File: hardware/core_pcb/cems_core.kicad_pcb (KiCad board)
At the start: 4 copper layers, 211.5 x 85.1 mm, 422 parts, among them J1 24VDC IN, J10 DIGITAL I/O IDC40, J11 BANK B, J13 FIELD 24V A+B, J15 PUMP, J17 RELAY COILS, J18 USB-C, J19 TEMP1, J2 CLIENT, J20 TEMP2, J21 TEMP3, J22 AI 1-2, J23 AI 3-4, J24 AI 5-6, J25 SENSORS, J3 I/O ONLY, J4 RVT70 RiBUS, J5 SWD, J6 SERVICE UART, J7 ROLE, Q1 2N7002, Q2 BC817, Q3 BC807, Q4 2N7002, Q5 BC817, Q6 BC807, SW1 RESET, U1 TPS54360B, U10 APS6404L, U11 MAX6369, U12 74LVC1G08, U13 74LVC1G175, U14 ISO2H823V2.5, U15 ISO808A-1, U16 ISO1I813T, U17 L78L05, U18 ISO7741, U19 74LVC1G08, U2 TLV62569DBV, U20 74LVC1G08, U21 IPS7091S, U22 74LVC1G14, U23 74LVC1G14, U24 LMV331, U25 CPC1017N, U26 CPC1017N, U27 USBLC6-2SC6, U28 ISOW7741, U29 74LVC1G04, U3 STM32H573VIT6, U30 ADS124S08, U31 ISOW7741, U32 74LVC1G04, U33 ITX2424SA, U34 AD4112, U35 L78L05, U36 LM317L, U37 REF5010, U38 LT3045, U4 LAN8742A-CZ, U5 TPD4E05U06, U6 W5500, U7 TPD4E05U06, U8 W25Q128JV, U9 MB85RC1MT, Y1 25MHz, Y2 32.768kHz, Y3 25MHz, Y4 25MHz

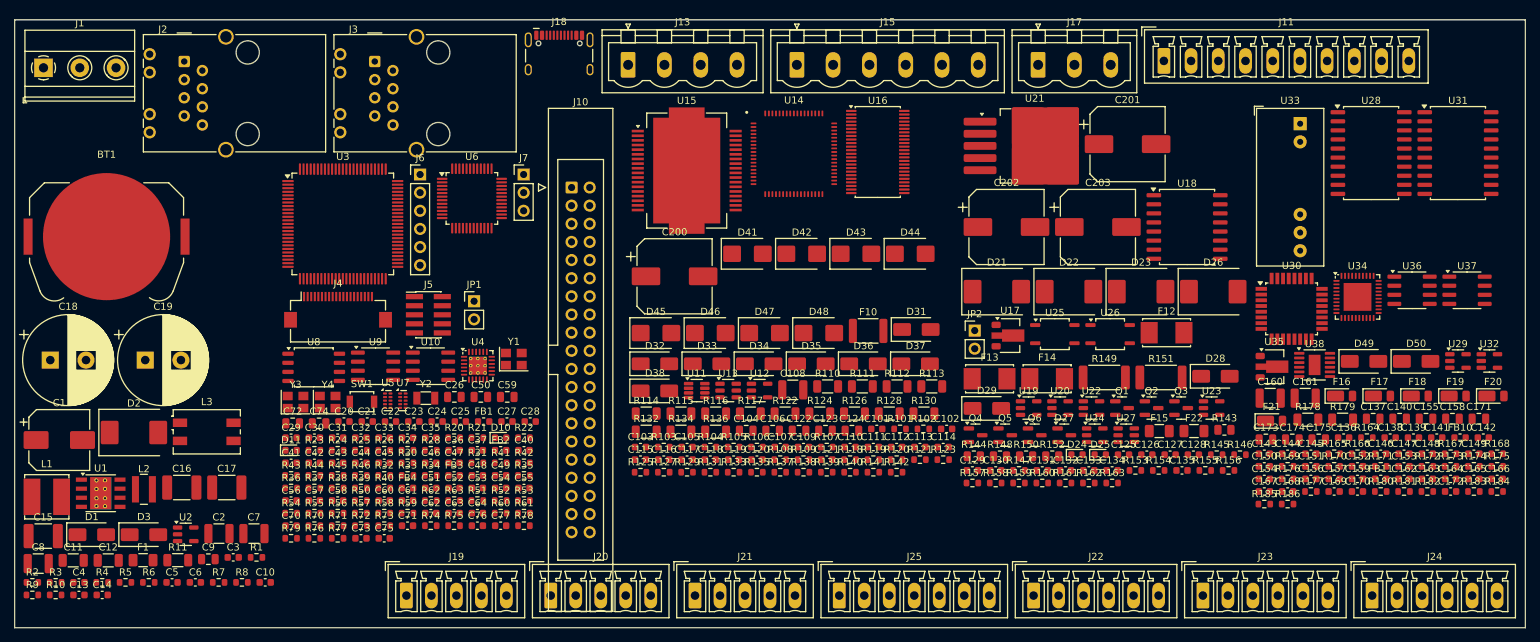
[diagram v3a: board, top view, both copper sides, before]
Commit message: CORE PCB: fit-optional 4 x 4-20 mA analog outputs (AD5755-1, all DNP)
AD5755-1 on the analog island with its own ISOW7741 (CS_AO on PD3) and an ITX2405SA for
the boost converters; keyed 8-way 3.5 mm J26 (keys 2, 6, script-checked). Pin numbers from
the datasheet Table 5. Layout block plan now 2.8 mm over in io_pwr: the board is full
single-sided, see thread for the module option.

Co-Authored-By: Claude Opus 5.5 <noreply@anthropic.com>
Claude-Session: https://claude.ai/code/session_014onnq3eRiDkqdAB6fKiRDW
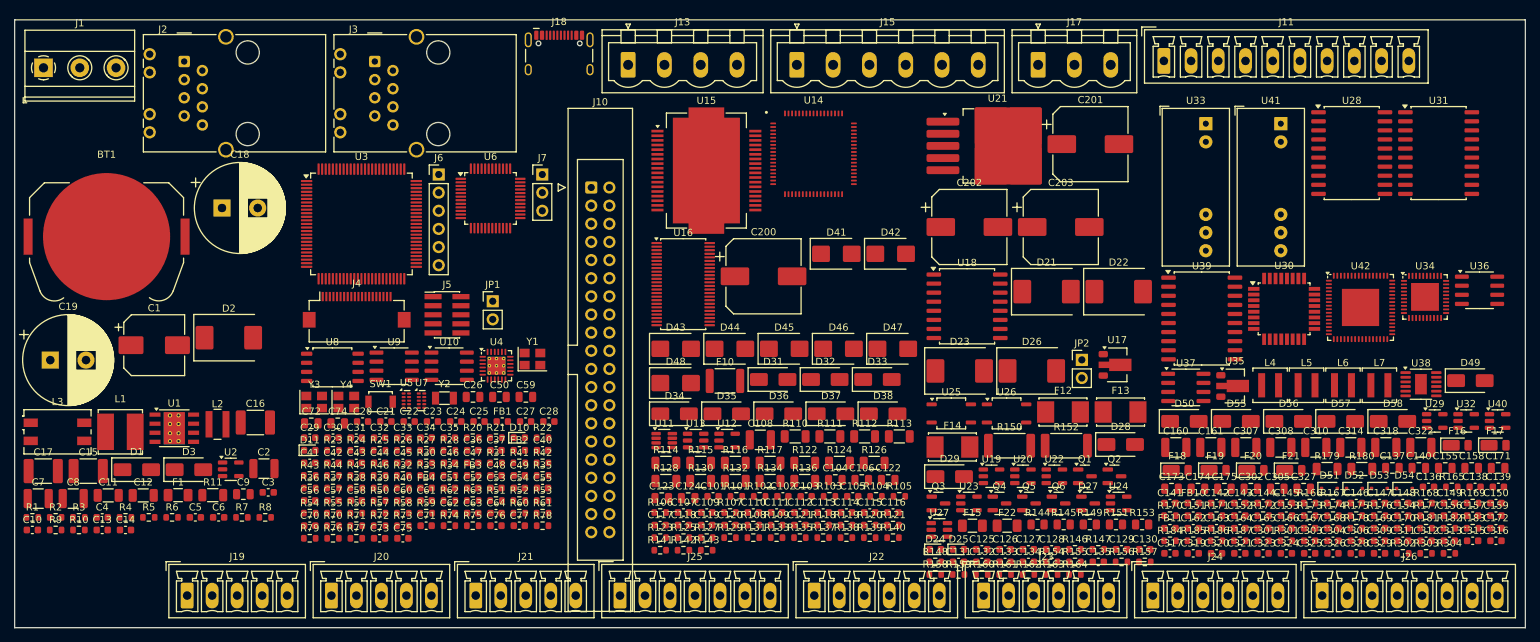
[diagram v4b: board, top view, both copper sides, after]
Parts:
- added C301: 100n, Capacitor_SMD:C_0603_1608Metric, F.Cu at (274.8, 172.9)
- added C302: 10u, Capacitor_SMD:C_0805_2012Metric, F.Cu at (273.1, 165.6)
- added C303: 100n, Capacitor_SMD:C_0603_1608Metric, F.Cu at (281.3, 172.9)
- added C304: 100n, Capacitor_SMD:C_0603_1608Metric, F.Cu at (284.6, 172.9)
- added C305: 10u, Capacitor_SMD:C_0805_2012Metric, F.Cu at (276.8, 165.6)
- added C306: 100n, Capacitor_SMD:C_0603_1608Metric, F.Cu at (287.8, 172.9)
- added C307: 10u 50V, Capacitor_SMD:C_1210_3225Metric, F.Cu at (272.4, 159.9)
- added C308: 22u, Capacitor_SMD:C_1210_3225Metric, F.Cu at (277.3, 159.9)
- added C309: 100n, Capacitor_SMD:C_0603_1608Metric, F.Cu at (291.1, 172.9)
- added C310: 4u7 50V, Capacitor_SMD:C_1210_3225Metric, F.Cu at (282.2, 159.9)
- added C311: 100n 50V, Capacitor_SMD:C_0603_1608Metric, F.Cu at (294.3, 172.9)
- added C312: 10n, Capacitor_SMD:C_0603_1608Metric, F.Cu at (297.6, 172.9)
- added C313: 4n7 50V, Capacitor_SMD:C_0603_1608Metric, F.Cu at (300.9, 172.9)
- added C314: 4u7 50V, Capacitor_SMD:C_1210_3225Metric, F.Cu at (287.1, 159.9)
- added C315: 100n 50V, Capacitor_SMD:C_0603_1608Metric, F.Cu at (304.1, 172.9)
- added C316: 10n, Capacitor_SMD:C_0603_1608Metric, F.Cu at (307.4, 172.9)
- added C317: 4n7 50V, Capacitor_SMD:C_0603_1608Metric, F.Cu at (261.7, 174.7)
- added C318: 4u7 50V, Capacitor_SMD:C_1210_3225Metric, F.Cu at (292.0, 159.9)
- added C319: 100n 50V, Capacitor_SMD:C_0603_1608Metric, F.Cu at (265.0, 174.7)
- added C320: 10n, Capacitor_SMD:C_0603_1608Metric, F.Cu at (268.3, 174.7)
- added C321: 4n7 50V, Capacitor_SMD:C_0603_1608Metric, F.Cu at (271.5, 174.7)
- added C322: 4u7 50V, Capacitor_SMD:C_1210_3225Metric, F.Cu at (296.9, 159.9)
- added C323: 100n 50V, Capacitor_SMD:C_0603_1608Metric, F.Cu at (274.8, 174.7)
- added C324: 10n, Capacitor_SMD:C_0603_1608Metric, F.Cu at (278.0, 174.7)
- added C325: 4n7 50V, Capacitor_SMD:C_0603_1608Metric, F.Cu at (281.3, 174.7)
- added C326: 100n, Capacitor_SMD:C_0603_1608Metric, F.Cu at (284.6, 174.7)
- added C327: 10u, Capacitor_SMD:C_0805_2012Metric, F.Cu at (280.5, 165.6)
- added C328: 100n 50V, Capacitor_SMD:C_0603_1608Metric, F.Cu at (287.8, 174.7)
- added C329: 100n, Capacitor_SMD:C_0603_1608Metric, F.Cu at (291.1, 174.7)
- added D51: PMEG4010, Diode_SMD:D_SOD-323F, F.Cu at (284.1, 165.6)
- added D52: PMEG4010, Diode_SMD:D_SOD-323F, F.Cu at (287.6, 165.6)
- added D53: PMEG4010, Diode_SMD:D_SOD-323F, F.Cu at (291.1, 165.6)
- added D54: PMEG4010, Diode_SMD:D_SOD-323F, F.Cu at (294.6, 165.6)
- added D55: SMAJ33A, Diode_SMD:D_SMA, F.Cu at (271.1, 156.2)
- added D56: SMAJ33A, Diode_SMD:D_SMA, F.Cu at (278.4, 156.2)
- added D57: SMAJ33A, Diode_SMD:D_SMA, F.Cu at (285.7, 156.2)
- added D58: SMAJ33A, Diode_SMD:D_SMA, F.Cu at (293.0, 156.2)
- added J26: AO 1-4, Connector_Phoenix_MC:PhoenixContact_MCV_1,5_8-G-3.5_1x08_P3.50mm_Vertical, F.Cu at (283.1, 180.6)
- added L4: 10uH, Inductor_SMD:L_Coilcraft_XAL4040-XXX, F.Cu at (275.8, 151.2)
- added L5: 10uH, Inductor_SMD:L_Coilcraft_XAL4040-XXX, F.Cu at (280.9, 151.2)
- added L6: 10uH, Inductor_SMD:L_Coilcraft_XAL4040-XXX, F.Cu at (286.0, 151.2)
- added L7: 10uH, Inductor_SMD:L_Coilcraft_XAL4040-XXX, F.Cu at (291.1, 151.2)
- added R187: 1M, Resistor_SMD:R_0603_1608Metric, F.Cu at (271.5, 172.9)
- added R301: 10k, Resistor_SMD:R_0603_1608Metric, F.Cu at (278.0, 172.9)
- added R302: 10k, Resistor_SMD:R_0603_1608Metric, F.Cu at (294.3, 174.7)
- added R303: 10k, Resistor_SMD:R_0603_1608Metric, F.Cu at (297.6, 174.7)
- added R304: 10k, Resistor_SMD:R_0603_1608Metric, F.Cu at (300.9, 174.7)
- added U39: ISOW7741, Package_SO:SOIC-20W_7.5x12.8mm_P1.27mm, F.Cu at (266.2, 141.8)
- added U40: 74LVC1G04, Package_TO_SOT_SMD:SOT-23-5, F.Cu at (307.6, 156.2)
- added U41: ITX2405SA, Converter_DCDC:Converter_DCDC_XP_POWER-ITXxxxxSA_THT, F.Cu at (277.3, 114.5)
- added U42: AD5755-1, Package_CSP:LFCSP-64-1EP_9x9mm_P0.5mm_EP5.21x5.21mm, F.Cu at (288.4, 140.3)
- R143, R148: footprint Resistor_SMD:R_0805_2012Metric -> Resistor_SMD:R_0603_1608Metric
- R145: value 100k -> 10k; footprint Resistor_SMD:R_0603_1608Metric -> Resistor_SMD:R_0805_2012Metric
- R147: value 10k -> 100k
- R149, R151: value 1k 1W -> 10k; footprint Resistor_SMD:R_2512_6332Metric -> Resistor_SMD:R_0805_2012Metric
- R150, R152: value 10k -> 1k 1W; footprint Resistor_SMD:R_0805_2012Metric -> Resistor_SMD:R_2512_6332Metric
- R153: footprint Resistor_SMD:R_0603_1608Metric -> Resistor_SMD:R_0805_2012Metric
- R154: value 4k3 -> 10k
- R155: value 10k -> 4k3
- R156: value 1M -> 10k
- R157: value 4k7 -> 1M
- R158: value 330R -> 4k7
- R160: value 5k1 -> 330R
- R162: value 33k -> 5k1
- R163: value 68k -> 33k
- R164: value 10k -> 68k
- R166: value 5k11 0.1% -> 10k
- R167: value 10M -> 5k11 0.1%
- R173: value 100R -> 10M
- R176: value 10k -> 100R
- R178: value 250R 0.1% -> 10k; footprint Resistor_SMD:R_1206_3216Metric -> Resistor_SMD:R_0603_1608Metric
- R180: value 100k -> 250R 0.1%; footprint Resistor_SMD:R_0603_1608Metric -> Resistor_SMD:R_1206_3216Metric
- R181: value 240R 1% -> 100k
- R182: value 2k26 1% -> 240R 1%
- R183: value 3k -> 2k26 1%
- R184: value 100k 0.1% -> 3k
- R186: value 1M -> 100k 0.1%
- moved R143 74.4 mm to (196.9, 174.2)
- moved R184 46.3 mm to (261.7, 172.9)
- moved R164 45.1 mm to (248.4, 177.6)
- moved U37 41.7 mm to (264.0, 151.5)
- moved R123 41.1 mm to (190.4, 172.5)
- moved C141 38.5 mm to (261.7, 167.6)
- moved C142 38.5 mm to (268.3, 167.6)
- moved FB10 38.5 mm to (265.0, 167.6)
- moved Q3 36.5 mm to (229.3, 167.7)
- moved U23 36.5 mm to (233.6, 167.7)
- moved F19 35.2 mm to (268.1, 163.1)
- moved F18 35.2 mm to (262.8, 163.1)
- moved F20 35.2 mm to (273.4, 163.1)
- moved D50 33.5 mm to (263.8, 156.2)
- moved C10 33.4 mm to (102.5, 171.4)
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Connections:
- R143 pad 1: +24V_FA -> +3V3
- R143 pad 2: FA_LED_A -> CS_AO
- R144 pad 1: +24V_FB -> +24V_FA
- R144 pad 2: FB_LED_A -> FA_LED_A
- R145 pad 1: PUMP_EN -> +24V_FB
- R145 pad 2: GND -> FB_LED_A
- R146 pad 1: PUMP_PWM -> PUMP_EN
- R147 pad 1: +5V_P -> PUMP_PWM
- R147 pad 2: P_DG -> GND
- R148 pad 1: +24V_FA -> +5V_P
- R148 pad 2: P_PWM_B -> P_DG
- R149 pad 1: P_PWM_E -> +24V_FA
- R149 pad 2: P_PWM_OUT -> P_PWM_B
- R150 pad 1: +24V_FA -> P_PWM_E
- R150 pad 2: P_DIR_B -> P_PWM_OUT
- R151 pad 1: P_DIR_E -> +24V_FA
- R151 pad 2: P_DIR_OUT -> P_DIR_B
- R152 pad 1: P_TACH_IN -> P_DIR_E
- R152 pad 2: P_TACH_C -> P_DIR_OUT
- R153 pad 1: +5V_P -> P_TACH_IN
- R153 pad 2: P_TREF -> P_TACH_C
- R154 pad 1: P_TREF -> +5V_P
- R154 pad 2: FIELD_0V -> P_TREF
- R155 pad 1: +5V_P -> P_TREF
- R155 pad 2: P_TACH_F -> FIELD_0V
- R156 pad 1: P_TACH_F -> +5V_P
- R156 pad 2: P_TACH_C -> P_TACH_F
- R157 pad 1: +5V_P -> P_TACH_F
- R157 pad 2: P_TACH_PU -> P_TACH_C
- R158 pad 1: GATE -> +5V_P
- R158 pad 2: REL1_A -> P_TACH_PU
- R159 pad 2: REL2_A -> REL1_A
- R160 pad 1: USB_CC1 -> GATE
- R160 pad 2: GND -> REL2_A
- R161 pad 1: USB_CC2 -> USB_CC1
- R162 pad 1: VBUS_USB -> USB_CC2
- R162 pad 2: USB_VBUS_SNS -> GND
- R163 pad 1: USB_VBUS_SNS -> VBUS_USB
- R163 pad 2: GND -> USB_VBUS_SNS
- R164 pad 1: +3V3 -> USB_VBUS_SNS
- R164 pad 2: T_ENFLT -> GND
- R165 pad 1: +3V3_T -> +3V3
- R165 pad 2: T_RST -> T_ENFLT
- R166 pad 1: T_REFP -> +3V3_T
- R166 pad 2: GND_T -> T_RST
- R167 pad 1: T1_N -> T_REFP
- R167 pad 2: T_AINCOM -> GND_T
- R168 pad 1: T2_N -> T1_N
- R169 pad 1: T3_N -> T2_N
- R170 pad 1: T4_N -> T3_N
- R171 pad 1: T5_N -> T4_N
- R172 pad 1: T6_N -> T5_N
- R173 pad 1: T_RTN1 -> T6_N
- R173 pad 2: T_REFP -> T_AINCOM
- R174 pad 1: T_RTN2 -> T_RTN1
- R175 pad 1: T_RTN3 -> T_RTN2
- R176 pad 1: +3V3 -> T_RTN3
- R176 pad 2: AI_ENFLT -> T_REFP
- R177 pad 1: +5V_AI -> +3V3
- R177 pad 2: AI_ERR -> AI_ENFLT
- R178 pad 1: AI5_IN -> +5V_AI
- R178 pad 2: GND_AI -> AI_ERR
- R179 pad 1: AI6_IN -> AI5_IN
- R180 pad 1: LVL_SIG -> AI6_IN
- R181 pad 1: +13V_AI -> LVL_SIG
- R181 pad 2: AI_ADJ -> GND_AI
- R182 pad 1: AI_ADJ -> +13V_AI
- R182 pad 2: GND_AI -> AI_ADJ
- R183 pad 1: FLOW_ILIM -> AI_ADJ
- R184 pad 1: +10V_FLOW -> FLOW_ILIM
- R184 pad 2: V10_MON -> GND_AI
- R185 pad 1: V10_MON -> +10V_FLOW
- R185 pad 2: GND_AI -> V10_MON
- R186 pad 1: FLOW_SIG -> V10_MON
- U3 pad 84: (no net) -> CS_AO

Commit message: CORE PCB: SPI expansion header J26 for plug-on modules; analog outputs move off the core
Gary: analog out as an add-on module. J26 10-way latched IDC: +24 V and +3.3 V behind PTCs,
SPI4 through 100R, MISO buffered by a 74LVC1G125 enabled by CS_EXP (PD3), EXP_INT on PD7.
The AD5755-1 block drafted in 04adb9f is removed from the core and will become the module.
Layout block plan fits again. CORE_PCB.md section 16.

Co-Authored-By: Claude Opus 5.5 <noreply@anthropic.com>
Claude-Session: https://claude.ai/code/session_014onnq3eRiDkqdAB6fKiRDW
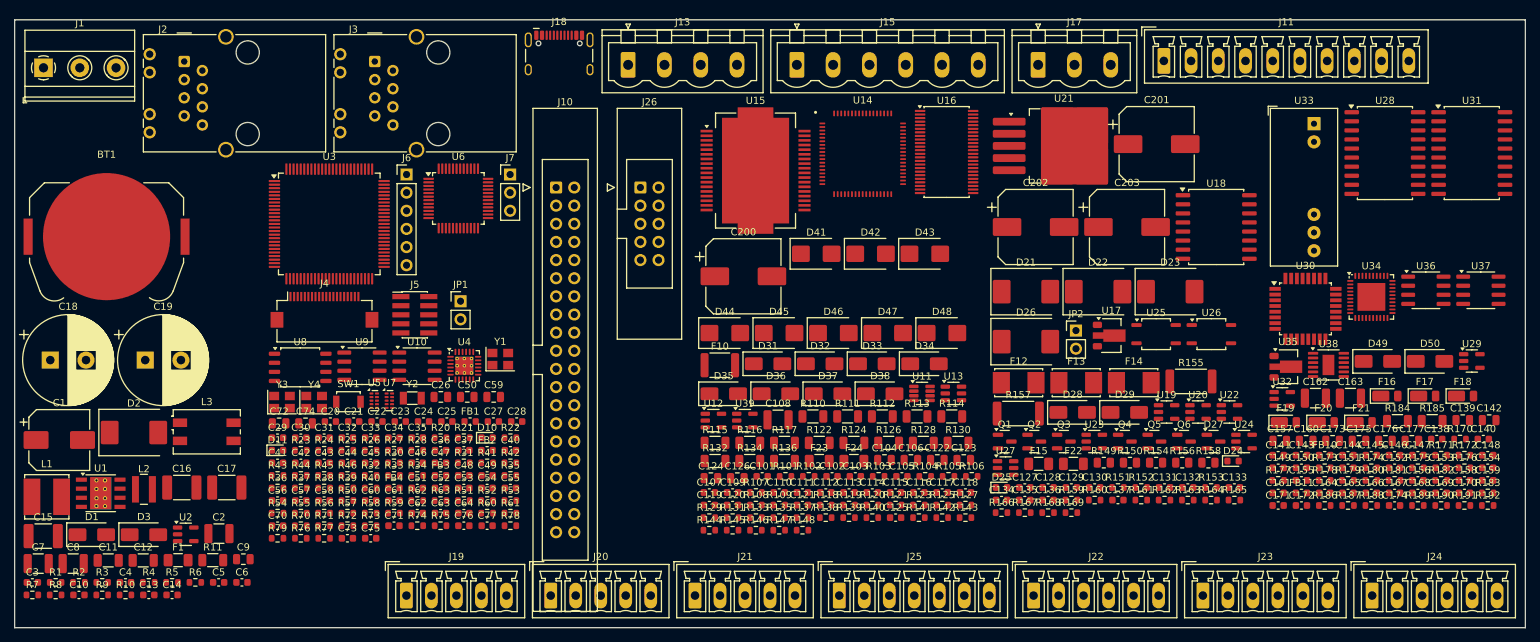
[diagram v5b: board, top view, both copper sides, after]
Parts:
- removed C301, C303, C304, C306, C309, C326, C329: 100n, Capacitor_SMD:C_0603_1608Metric
- removed C302, C305, C327: 10u, Capacitor_SMD:C_0805_2012Metric
- removed C307: 10u 50V, Capacitor_SMD:C_1210_3225Metric
- removed C308: 22u, Capacitor_SMD:C_1210_3225Metric
- removed C310, C314, C318, C322: 4u7 50V, Capacitor_SMD:C_1210_3225Metric
- removed C311, C315, C319, C323, C328: 100n 50V, Capacitor_SMD:C_0603_1608Metric
- removed C312, C316, C320, C324: 10n, Capacitor_SMD:C_0603_1608Metric
- removed C313, C317, C321, C325: 4n7 50V, Capacitor_SMD:C_0603_1608Metric
- removed D51, D52, D53, D54: PMEG4010, Diode_SMD:D_SOD-323F
- removed D55, D56, D57, D58: SMAJ33A, Diode_SMD:D_SMA
- removed L4, L5, L6, L7: 10uH, Inductor_SMD:L_Coilcraft_XAL4040-XXX
- removed R301, R302, R303, R304: 10k, Resistor_SMD:R_0603_1608Metric
- removed U40: 74LVC1G04, Package_TO_SOT_SMD:SOT-23-5
- removed U41: ITX2405SA, Converter_DCDC:Converter_DCDC_XP_POWER-ITXxxxxSA_THT
- removed U42: AD5755-1, Package_CSP:LFCSP-64-1EP_9x9mm_P0.5mm_EP5.21x5.21mm
- added C176: 4u7 25V, Capacitor_SMD:C_0805_2012Metric, F.Cu at (291.9, 158.9)
- added C177: 10u 25V, Capacitor_SMD:C_0805_2012Metric, F.Cu at (295.6, 158.9)
- added F23: 0.5A, Fuse:Fuse_1206_3216Metric, F.Cu at (212.6, 161.8)
- added F24: 0.1A, Fuse:Fuse_1206_3216Metric, F.Cu at (217.5, 161.8)
- added R188: 2k26 1%, Resistor_SMD:R_0603_1608Metric, F.Cu at (289.9, 168.0)
- added R189: 3k, Resistor_SMD:R_0603_1608Metric, F.Cu at (296.5, 168.0)
- added R190: 100k 0.1%, Resistor_SMD:R_0603_1608Metric, F.Cu at (299.7, 168.0)
- added R191: 100k 0.1%, Resistor_SMD:R_0603_1608Metric, F.Cu at (303.0, 168.0)
- added R192: 1M, Resistor_SMD:R_0603_1608Metric, F.Cu at (306.2, 168.0)
- C125: value 330n 50V -> 100n
- C126: value 1u -> 100n; footprint Capacitor_SMD:C_0603_1608Metric -> Capacitor_SMD:C_0805_2012Metric
- C127: value 100n -> 330n 50V
- C128, C147: value 100n -> 1u
- C131: value 100n 50V -> 100n
- C133: value 100n -> 100n 50V
- C134: value 1n -> 100n
- C136: value 100n -> 1n
- C137, C140, C158: value 10u -> 100n; footprint Capacitor_SMD:C_0805_2012Metric -> Capacitor_SMD:C_0603_1608Metric
- C139, C142, C157: value 100n -> 10u; footprint Capacitor_SMD:C_0603_1608Metric -> Capacitor_SMD:C_0805_2012Metric
- C143, C170: value 1u -> 100n
- C148, C149: value 10n C0G -> 100n
- C154: value 100n -> 10n C0G
- C155: value 10u -> 10n C0G; footprint Capacitor_SMD:C_0805_2012Metric -> Capacitor_SMD:C_0603_1608Metric
- C160: value 10u 50V -> 10u; footprint Capacitor_SMD:C_1210_3225Metric -> Capacitor_SMD:C_0805_2012Metric
- C161: value 10u 50V -> 100n; footprint Capacitor_SMD:C_1210_3225Metric -> Capacitor_SMD:C_0603_1608Metric
- C162: value 100n -> 10u 50V; footprint Capacitor_SMD:C_0603_1608Metric -> Capacitor_SMD:C_1210_3225Metric
- C163: value 1u -> 10u 50V; footprint Capacitor_SMD:C_0603_1608Metric -> Capacitor_SMD:C_1210_3225Metric
- C169: value 330n 50V -> 1u
- C171: value 1u 25V -> 330n 50V; footprint Capacitor_SMD:C_0805_2012Metric -> Capacitor_SMD:C_0603_1608Metric
- C174: value 4u7 25V -> 1u; footprint Capacitor_SMD:C_0805_2012Metric -> Capacitor_SMD:C_0603_1608Metric
- C175: value 10u 25V -> 1u 25V
- J26: value AO 1-4 -> SPI EXPANSION; footprint Connector_Phoenix_MC:PhoenixContact_MCV_1,5_8-G-3.5_1x08_P3.50mm_Vertical -> Connector_IDC:IDC-Header_2x05_P2.54mm_Latch_Vertical
- R138, R139, R140: value 10k -> 100R
- R141: value 10k -> 100k
- R144, R145, R153: footprint Resistor_SMD:R_0805_2012Metric -> Resistor_SMD:R_0603_1608Metric
- R146, R147: value 100k -> 10k
- R150: value 1k 1W -> 10k; footprint Resistor_SMD:R_2512_6332Metric -> Resistor_SMD:R_0805_2012Metric
- R151: value 10k -> 100k; footprint Resistor_SMD:R_0805_2012Metric -> Resistor_SMD:R_0603_1608Metric
- R152: value 1k 1W -> 100k; footprint Resistor_SMD:R_2512_6332Metric -> Resistor_SMD:R_0603_1608Metric
- R154, R156: footprint Resistor_SMD:R_0603_1608Metric -> Resistor_SMD:R_0805_2012Metric
- R155: value 4k3 -> 1k 1W; footprint Resistor_SMD:R_0603_1608Metric -> Resistor_SMD:R_2512_6332Metric
- R157: value 1M -> 1k 1W; footprint Resistor_SMD:R_0603_1608Metric -> Resistor_SMD:R_2512_6332Metric
- R158: value 4k7 -> 10k; footprint Resistor_SMD:R_0603_1608Metric -> Resistor_SMD:R_0805_2012Metric
- R159: value 330R -> 10k
- R160: value 330R -> 4k3
- R161: value 5k1 -> 10k
- R162: value 5k1 -> 1M
- R163: value 33k -> 4k7
- R164: value 68k -> 330R
- R165: value 10k -> 330R
- R166: value 10k -> 5k1
- R167: value 5k11 0.1% -> 5k1
- R168: value 10M -> 33k
- R169: value 10M -> 68k
- R170, R171: value 10M -> 10k
- R172: value 10M -> 5k11 0.1%
- R174, R175, R176: value 100R -> 10M
- R177, R178: value 10k -> 10M
- R179, R180: value 250R 0.1% -> 100R; footprint Resistor_SMD:R_1206_3216Metric -> Resistor_SMD:R_0603_1608Metric
- R181: value 100k -> 100R
- R182: value 240R 1% -> 10k
- R183: value 2k26 1% -> 10k
- R184: value 3k -> 250R 0.1%; footprint Resistor_SMD:R_0603_1608Metric -> Resistor_SMD:R_1206_3216Metric
- R185: value 100k 0.1% -> 250R 0.1%; footprint Resistor_SMD:R_0603_1608Metric -> Resistor_SMD:R_1206_3216Metric
- R186: value 100k 0.1% -> 100k
- R187: value 1M -> 240R 1%
- U39: value ISOW7741 -> 74LVC1G125; footprint Package_SO:SOIC-20W_7.5x12.8mm_P1.27mm -> Package_TO_SOT_SMD:SOT-23-5
- moved J26 111.2 mm to (187.6, 123.5)
- moved U39 65.5 mm to (202.2, 156.1)
- moved R169 56.2 mm to (247.9, 169.0)
- moved C136 53.3 mm to (244.7, 167.2)
- moved R168 52.9 mm to (244.7, 169.0)
- moved R145 46.4 mm to (200.5, 171.4)
- moved R144 46.0 mm to (197.3, 171.4)
- moved R146 44.8 mm to (203.8, 171.4)
- moved R147 44.8 mm to (207.0, 171.4)
- moved R106 43.9 mm to (234.0, 163.9)
- moved D24 43.5 mm to (270.6, 161.8)
- moved U37 43.5 mm to (305.3, 137.9)
- moved R166 43.2 mm to (238.2, 169.0)
- moved R167 43.2 mm to (241.4, 169.0)
- moved C123 42.6 mm to (232.9, 161.6)
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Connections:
- C125 pad 1: +24V_FA -> +3V3
- C125 pad 2: FIELD_0V -> GND
- C126 pad 1: +5V_P -> +24V_EXP
- C126 pad 2: FIELD_0V -> GND
- C127 pad 1: +3V3 -> +24V_FA
- C127 pad 2: GND -> FIELD_0V
- C128 pad 1: +3V3 -> +5V_P
- C128 pad 2: GND -> FIELD_0V
- C130 pad 1: +5V_P -> +3V3
- C130 pad 2: FIELD_0V -> GND
- C131 pad 1: +24V_FP -> +3V3
- C131 pad 2: FIELD_0V -> GND
- C133 pad 1: +5V_P -> +24V_FP
- C134 pad 1: P_TACH_C -> +5V_P
- C136 pad 1: +3V3 -> P_TACH_C
- C136 pad 2: GND -> FIELD_0V
- C137 pad 1: +5V -> +5V_P
- C137 pad 2: GND -> FIELD_0V
- C138 pad 1: +5V -> +3V3
- C139 pad 1: +3V3 -> +5V
- C140 pad 1: +3V3_T -> +5V
- C140 pad 2: GND_T -> GND
- C141 pad 1: +3V3_T -> +3V3
- C141 pad 2: GND_T -> GND
- C143 pad 1: +3V3_TA -> +3V3_T
- C144 pad 1: +3V3_TA -> +3V3_T
- C145 pad 1: T_REFOUT -> +3V3_TA
- C146 pad 1: T_REFP -> +3V3_TA
- C147 pad 1: T_AINCOM -> T_REFOUT
- C148 pad 1: T1_P -> T_REFP
- C148 pad 2: T1_N -> GND_T
- C149 pad 1: T2_P -> T_AINCOM
- C149 pad 2: T2_N -> GND_T
- C150 pad 1: T3_P -> T1_P
- C150 pad 2: T3_N -> T1_N
- C151 pad 1: T4_P -> T2_P
- C151 pad 2: T4_N -> T2_N
- C152 pad 1: T5_P -> T3_P
- C152 pad 2: T5_N -> T3_N
- C153 pad 1: T6_P -> T4_P
- C153 pad 2: T6_N -> T4_N
- C154 pad 1: +3V3 -> T5_P
- C154 pad 2: GND -> T5_N
- C155 pad 1: +5V -> T6_P
- C155 pad 2: GND -> T6_N
- C156 pad 1: +5V -> +3V3
- C157 pad 1: +3V3 -> +5V
- C158 pad 1: +5V_AI -> +5V
- C158 pad 2: GND_AI -> GND
- C159 pad 1: +5V_AI -> +3V3
- C159 pad 2: GND_AI -> GND
- C160 pad 1: +24V -> +5V_AI
- C160 pad 2: GND -> GND_AI
- C161 pad 1: +24V_AI -> +5V_AI
- C162 pad 1: +5V_AI -> +24V
- C162 pad 2: GND_AI -> GND
- C163 pad 1: +5V_AIA -> +24V_AI
- C164 pad 1: +5V_AIA -> +5V_AI
- C165 pad 1: AI_REGCAPA -> +5V_AIA
- C166 pad 1: AI_REGCAPA -> +5V_AIA
- C167 pad 1: AI_REGCAPD -> AI_REGCAPA
- C168 pad 1: AI_REF -> AI_REGCAPA
- C169 pad 1: +24V_AI -> AI_REGCAPD
- C170 pad 1: +5V_LVL -> AI_REF
- C171 pad 1: +13V_AI -> +24V_AI
- C172 pad 1: REF10_NR -> +5V_LVL
- C173 pad 1: REF10 -> +13V_AI
- C174 pad 1: +13V_AI -> REF10_NR
- C175 pad 1: +10V_FLOW -> REF10
- J26 pad 1: AO_IOUT1 -> +24V_EXP
- J26 pad 2: GND_AI -> GND
- J26 pad 3: AO_IOUT2 -> +3V3_EXP
- J26 pad 4: GND_AI -> GND
- J26 pad 5: AO_IOUT3 -> EXP_SCK
- J26 pad 6: GND_AI -> GND
- J26 pad 7: AO_IOUT4 -> EXP_MOSI
- J26 pad 8: GND_AI -> EXP_MISO
- R138 pad 1: +3V3 -> SPI4_SCK
- R138 pad 2: CS_A -> EXP_SCK
- R139 pad 1: +3V3 -> SPI4_MOSI
- R139 pad 2: CS_B -> EXP_MOSI
- R140 pad 1: +3V3 -> CS_EXP
- R140 pad 2: CS_IN -> EXP_CS
- R141 pad 1: +3V3 -> EXP_MISO
- R141 pad 2: CS_T -> GND
- R142 pad 2: CS_AI -> EXP_INT
- R143 pad 2: CS_AO -> CS_A
- R144 pad 1: +24V_FA -> +3V3
- R144 pad 2: FA_LED_A -> CS_B
- R145 pad 1: +24V_FB -> +3V3
- R145 pad 2: FB_LED_A -> CS_IN
- R146 pad 1: PUMP_EN -> +3V3
- R146 pad 2: GND -> CS_T
- R147 pad 1: PUMP_PWM -> +3V3
- R147 pad 2: GND -> CS_AI
- R148 pad 1: +5V_P -> +3V3
- R148 pad 2: P_DG -> CS_EXP
- R149 pad 2: P_PWM_B -> FA_LED_A
- R150 pad 1: P_PWM_E -> +24V_FB
- R150 pad 2: P_PWM_OUT -> FB_LED_A
- R151 pad 1: +24V_FA -> PUMP_EN
- R151 pad 2: P_DIR_B -> GND
- R152 pad 1: P_DIR_E -> PUMP_PWM
- R152 pad 2: P_DIR_OUT -> GND
- R153 pad 1: P_TACH_IN -> +5V_P
- R153 pad 2: P_TACH_C -> P_DG
- R154 pad 1: +5V_P -> +24V_FA
- R154 pad 2: P_TREF -> P_PWM_B
- R155 pad 1: P_TREF -> P_PWM_E
- R155 pad 2: FIELD_0V -> P_PWM_OUT
- R156 pad 1: +5V_P -> +24V_FA
- R156 pad 2: P_TACH_F -> P_DIR_B
- R157 pad 1: P_TACH_F -> P_DIR_E
- R157 pad 2: P_TACH_C -> P_DIR_OUT
- R158 pad 1: +5V_P -> P_TACH_IN
- R158 pad 2: P_TACH_PU -> P_TACH_C
- R159 pad 1: GATE -> +5V_P
- R159 pad 2: REL1_A -> P_TREF
- R160 pad 1: GATE -> P_TREF
- R160 pad 2: REL2_A -> FIELD_0V
- R161 pad 1: USB_CC1 -> +5V_P
- R161 pad 2: GND -> P_TACH_F
- R162 pad 1: USB_CC2 -> P_TACH_F
- R162 pad 2: GND -> P_TACH_C
- R163 pad 1: VBUS_USB -> +5V_P
- R163 pad 2: USB_VBUS_SNS -> P_TACH_PU
- R164 pad 1: USB_VBUS_SNS -> GATE
- R164 pad 2: GND -> REL1_A
- R165 pad 1: +3V3 -> GATE
- R165 pad 2: T_ENFLT -> REL2_A
- R166 pad 1: +3V3_T -> USB_CC1
- R166 pad 2: T_RST -> GND
- R167 pad 1: T_REFP -> USB_CC2
- R167 pad 2: GND_T -> GND
- R168 pad 1: T1_N -> VBUS_USB
- R168 pad 2: T_AINCOM -> USB_VBUS_SNS
- R169 pad 1: T2_N -> USB_VBUS_SNS
- R169 pad 2: T_AINCOM -> GND
- R170 pad 1: T3_N -> +3V3
- R170 pad 2: T_AINCOM -> T_ENFLT
- R171 pad 1: T4_N -> +3V3_T
- R171 pad 2: T_AINCOM -> T_RST
- R172 pad 1: T5_N -> T_REFP
- R172 pad 2: T_AINCOM -> GND_T
- R173 pad 1: T6_N -> T1_N
- R174 pad 1: T_RTN1 -> T2_N
- R174 pad 2: T_REFP -> T_AINCOM
- R175 pad 1: T_RTN2 -> T3_N
- R175 pad 2: T_REFP -> T_AINCOM
- R176 pad 1: T_RTN3 -> T4_N
- R176 pad 2: T_REFP -> T_AINCOM
- R177 pad 1: +3V3 -> T5_N
- R177 pad 2: AI_ENFLT -> T_AINCOM
- R178 pad 1: +5V_AI -> T6_N
- R178 pad 2: AI_ERR -> T_AINCOM
- R179 pad 1: AI5_IN -> T_RTN1
- R179 pad 2: GND_AI -> T_REFP
- R180 pad 1: AI6_IN -> T_RTN2
- R180 pad 2: GND_AI -> T_REFP
- R181 pad 1: LVL_SIG -> T_RTN3
- R181 pad 2: GND_AI -> T_REFP
- R182 pad 1: +13V_AI -> +3V3
- R182 pad 2: AI_ADJ -> AI_ENFLT
- R183 pad 1: AI_ADJ -> +5V_AI
- R183 pad 2: GND_AI -> AI_ERR
- R184 pad 1: FLOW_ILIM -> AI5_IN
- R185 pad 1: +10V_FLOW -> AI6_IN
- R185 pad 2: V10_MON -> GND_AI
- R186 pad 1: V10_MON -> LVL_SIG
- R187 pad 1: FLOW_SIG -> +13V_AI
- R187 pad 2: GND_AI -> AI_ADJ
- U3 pad 84: CS_AO -> CS_EXP
- U3 pad 88: (no net) -> EXP_INT
- U39 pad 1: +3V3 -> CS_EXP
- U39 pad 2: SPI4_SCK -> EXP_MISO
- U39 pad 3: SPI4_MOSI -> GND
- U39 pad 4: CS_AO -> SPI4_MISO
- U39 pad 5: SPI4_MISO -> +3V3

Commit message: CORE PCB: placement by isolation domain, planes and isolation keep-outs, routing script, AU BOM
autolayout.py places all 434 parts: domain floor plan (logic left + strip, field top right,
temperature and analog islands bottom right), isolators straddling straight boundaries,
IC clusters placed near their connections, no courtyard overlaps. In1 ground plane per
domain, In2 +24V_FA plane, 2.5 mm keep-out strips. Net classes reworked (HICURRENT 1 mm,
RAIL, OUT1A). route.py (Freerouting via DSN/SES + DRC), plot_board.py, bom_au.py.

Co-Authored-By: Claude Opus 5.5 <noreply@anthropic.com>
Claude-Session: https://claude.ai/code/session_014onnq3eRiDkqdAB6fKiRDW
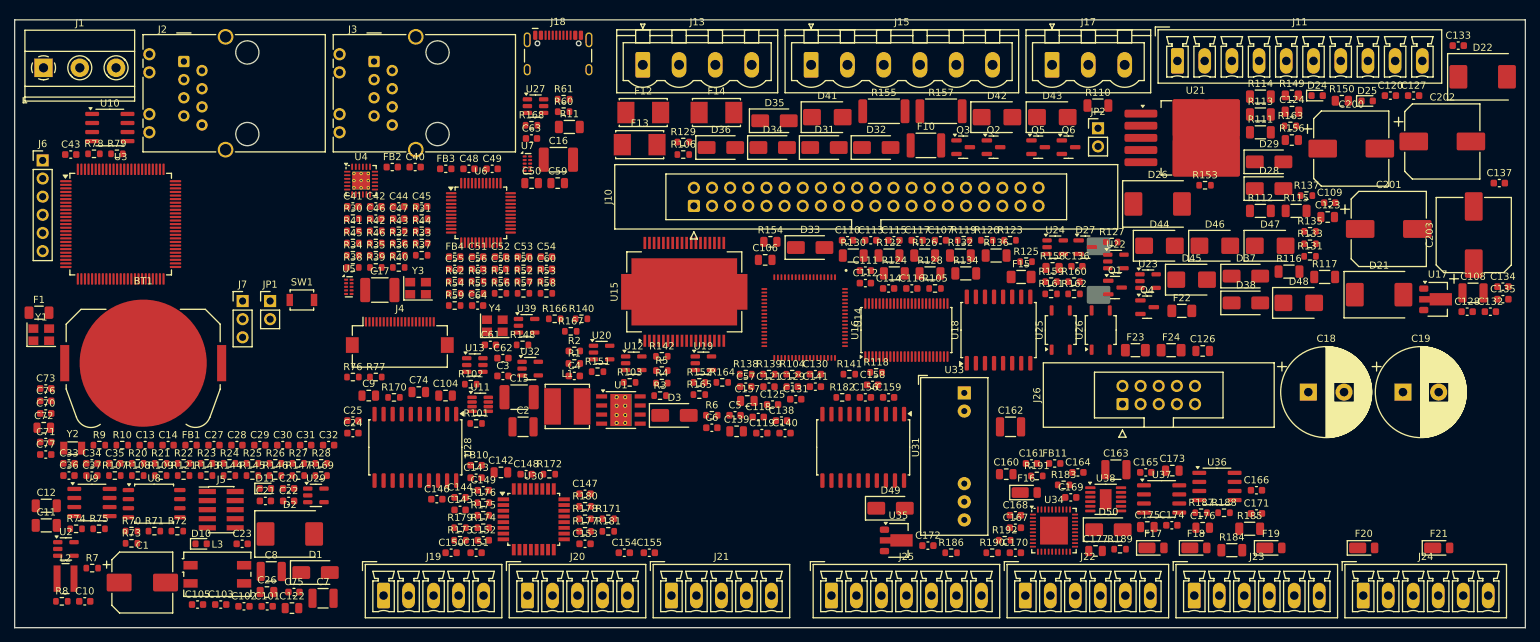
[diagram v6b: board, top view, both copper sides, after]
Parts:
- D23: moved to B.Cu
- moved C18 176.2 mm to (281.1, 152.1)
- moved C19 176.1 mm to (294.4, 152.1)
- moved U29 162.9 mm to (142.2, 166.6)
- moved R170 149.4 mm to (153.1, 152.9)
- moved U28 141.9 mm to (156.1, 159.9), turned to -90 degrees
- moved C142 138.6 mm to (168.1, 163.4)
- moved R176 137.5 mm to (165.6, 167.6)
- moved C148 134.7 mm to (171.6, 163.6)
- moved C146 134.2 mm to (159.1, 167.1)
- moved R175 131.0 mm to (165.6, 169.4)
- moved R172 128.1 mm to (174.9, 163.6)
- moved C152 128.0 mm to (165.6, 172.9)
- moved C145 127.8 mm to (162.4, 168.6)
- moved R174 124.6 mm to (165.6, 171.1)
- moved R179 124.5 mm to (162.4, 171.1)
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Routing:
- added copper zone on In2.Cu, net +24V_FA
- added copper zone on In1.Cu, net FIELD_0V
- added copper zone on In1.Cu, net GND
- added copper zone on In1.Cu, net GND_AI
- added copper zone on In1.Cu, net GND_T
